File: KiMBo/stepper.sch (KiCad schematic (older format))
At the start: 25 parts

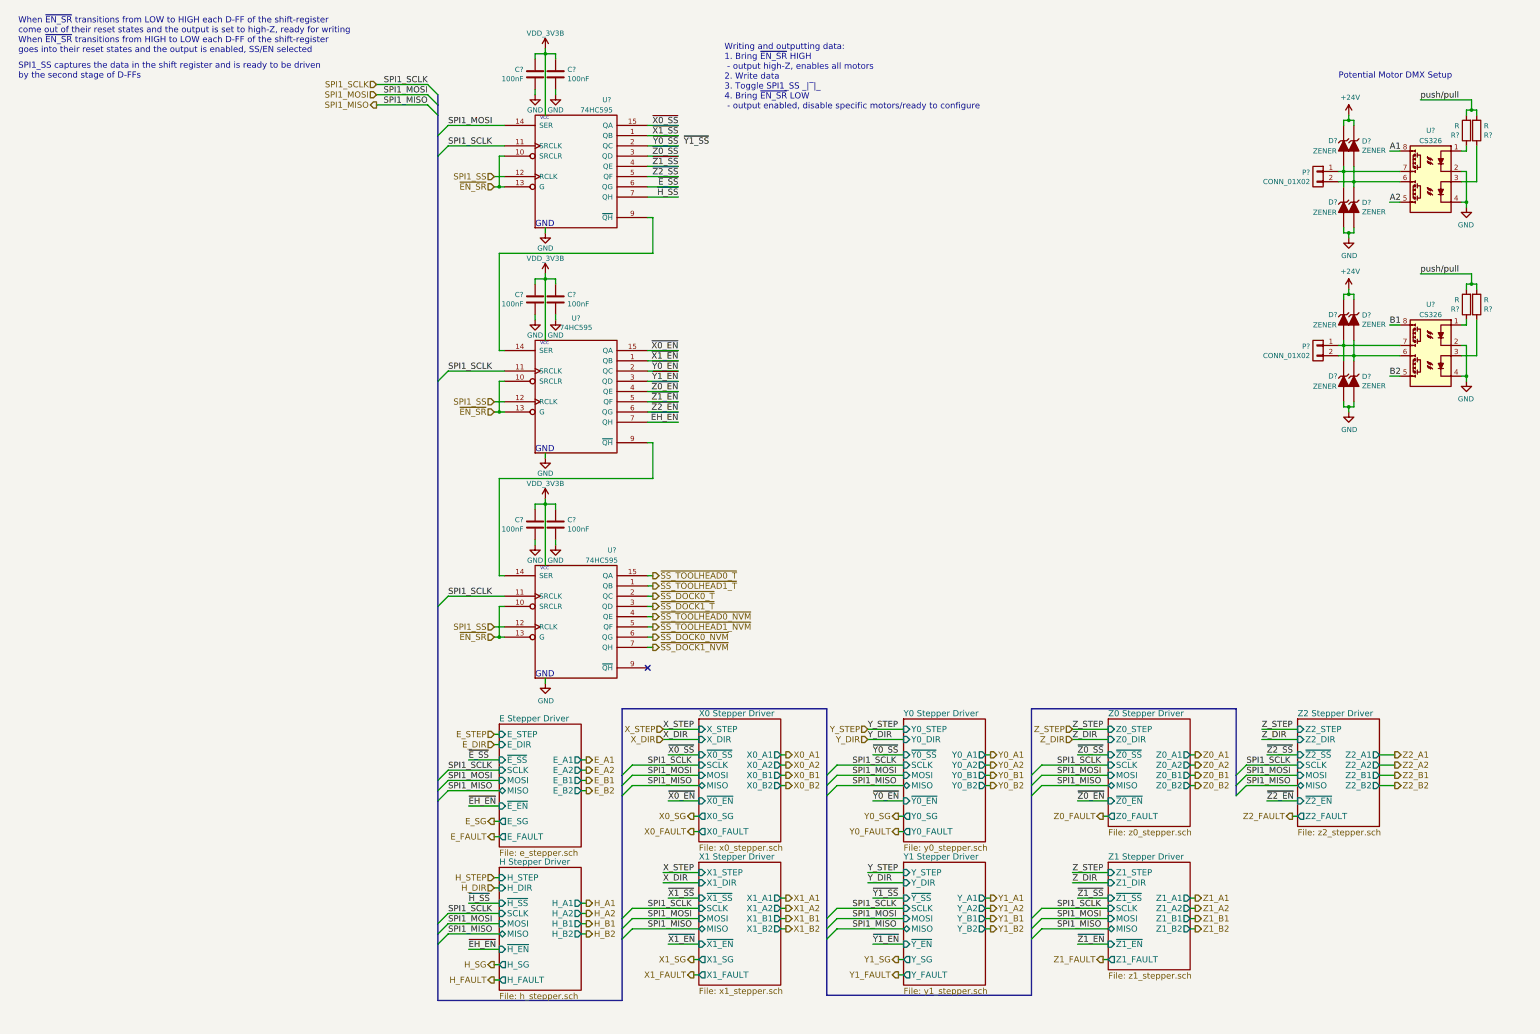
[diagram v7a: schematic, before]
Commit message: Use only one driver on Y, NAND X and Z FAULT and SG signals
Dual X carriage will need to be tested to determine if two seperate drivers are required for X
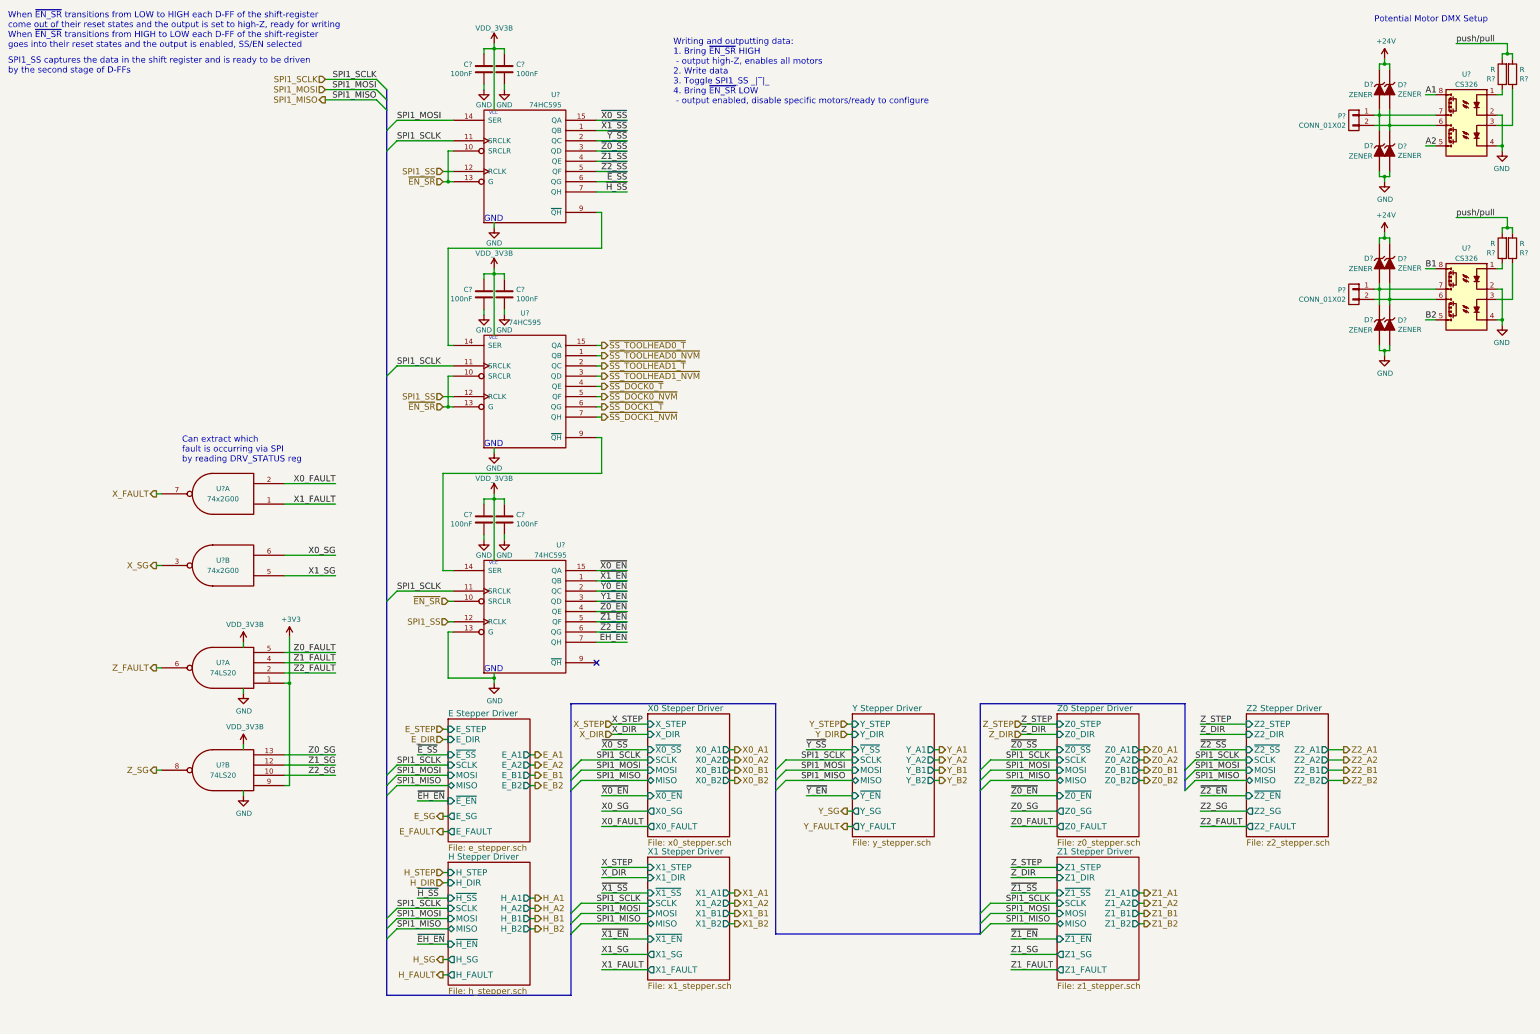
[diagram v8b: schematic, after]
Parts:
- added U? (x2): 74LS20, symbol 74LS20
- added U? (x2): 74x2G00, symbol 74x2G00
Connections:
- net VCC is gone; now on net GND: C?.1, C?.1, C?.1, C?.1, C?.1, C?.2, U?.16 (VCC), U?.16 (VCC), U?.16 (VCC)
- net GND: now also U?.13 (G), U?.14 (VCC), U?.14 (VCC), U?.4 (GND), U?.4 (GND), U?.7 (GND), U?.7 (GND), U?.8 (VCC), U?.8 (VCC)
- net X0_FAULT: now also U?.2
- net X0_SG: now also U?.6
- net X1_FAULT: now also U?.1
- net X1_SG: now also U?.5
- net Z0_FAULT: now also U?.5
- net Z1_FAULT: now also U?.4
- net Z2_FAULT: now also U?.2
- net ~EH_EN: now also U?.7 (QH); no longer U?.7 (QH)
- net ~EN_SR: no longer U?.13 (G)
- net ~SS_DOCK0_NVM: now also U?.5 (QF); no longer U?.6 (QG)
- net ~SS_DOCK0_T: now also U?.4 (QE); no longer U?.2 (QC)
- net ~SS_DOCK1_NVM: now also U?.7 (QH); no longer U?.7 (QH)
- net ~SS_DOCK1_T: now also U?.6 (QG); no longer U?.3 (QD)
- net ~SS_TOOLHEAD0_NVM: now also U?.1 (QB); no longer U?.4 (QE)
- net ~SS_TOOLHEAD0_T: now also U?.15 (QA); no longer U?.15 (QA)
- net ~SS_TOOLHEAD1_NVM: now also U?.3 (QD); no longer U?.5 (QF)
- net ~SS_TOOLHEAD1_T: now also U?.2 (QC); no longer U?.1 (QB)
- net ~X0_EN: now also U?.15 (QA); no longer U?.15 (QA)
- net ~X1_EN: now also U?.1 (QB); no longer U?.1 (QB)
- net ~Y0_EN: now also U?.2 (QC); no longer U?.2 (QC)
- net ~Y1_EN: now also U?.3 (QD); no longer U?.3 (QD)
- net ~Z0_EN: now also U?.4 (QE); no longer U?.4 (QE)
- net ~Z1_EN: now also U?.5 (QF); no longer U?.5 (QF)
- net ~Z2_EN: now also U?.6 (QG); no longer U?.6 (QG)
- net ~Y0_SS renamed ~Y_SS
- new net +3V3: U?.1, U?.9
- new net X_FAULT: U?.7
- new net X_SG: U?.3
- new net Z0_SG: U?.13
- new net Z1_SG: U?.12
- new net Z2_SG: U?.10
- new net Z_FAULT: U?.6
- new net Z_SG: U?.8
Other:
- note added: "Can extract which\nfault is occurring via SPI\nby reading DRV_STATUS reg"
- moved on the sheet: C?, D?, P?, R?, U?
